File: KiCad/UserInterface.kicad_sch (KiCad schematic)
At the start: 0 parts

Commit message: Filled in schematic
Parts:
- added C13, C14, C15, C16, C17, C18, C19: C, symbol Device:C
- added D4, D5: LED, symbol Device:LED
- added J3: Btn_Menu_Conn, symbol Connector:Conn_01x06_Socket
- added J4: Btn_Matrix_Conn, symbol Connector:Conn_01x08_Socket
- added J5: Enc_Conn, Connector_PinHeader_2.54mm:PinHeader_1x03_P2.54mm_Vertical, symbol Connector:Conn_01x03_Socket
- added J6: Pwr_Conn, symbol Connector:Conn_01x02_Socket
- added J7: LCD_Conn, Connector_PinHeader_2.54mm:PinHeader_1x03_P2.54mm_Vertical, symbol Connector:Conn_01x03_Socket
- added R29, R30, R31, R32, R33, R34, R35: 10k, symbol Device:R
- added R36, R37: 1k, symbol Device:R
- added SW1, SW18, SW20, SW21: SW_Push, symbol Switch:SW_Push
- added SW10, SW11, SW12, SW13, SW14, SW15, SW16, SW17, SW2, SW3, SW4, SW5, SW6, SW7, SW8, SW9: SW_Push_45deg, symbol Switch:SW_Push_45deg
- added SW19: RotaryEncoder_Switch, symbol Device:RotaryEncoder_Switch
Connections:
- new net: SW13.1, SW17.1, SW5.1, SW9.1
- new net: SW14.2, SW15.2, SW16.2, SW17.2
- new net: SW11.1, SW15.1, SW3.1, SW7.1
- new net: SW10.2, SW11.2, SW12.2, SW13.2
- new net: SW12.1, SW16.1, SW4.1, SW8.1
- new net: SW2.2, SW3.2, SW4.2, SW5.2
- new net: D4.2 (A), R37.2
- new net: SW6.2, SW7.2, SW8.2, SW9.2
- new net: D5.2 (A), R36.2
- new net +3V3: J6.1 (Pin_1), R29.1, R30.1, R31.1, R32.1, R33.1, R34.1, R35.1
- new net ENC_CLK: C14.1, J5.1 (Pin_1), R30.2, SW19.A
- new net ENC_DT: C15.1, J5.2 (Pin_2), R31.2, SW19.B
- new net ENC_SW: C13.1, J5.3 (Pin_3), R29.2, SW19.S1
- new net GND: C13.2, C14.2, C15.2, C16.2, C17.2, C18.2, C19.2, D4.1 (K), D5.1 (K), J6.2 (Pin_2), SW1.1, SW18.1, SW19.C, SW19.S2, SW20.1, SW21.1
- new net LED1_IN: J3.5 (Pin_5), R37.1
- new net LED2_IN: J3.6 (Pin_6), R36.1
- new net SW1_OUT: C16.1, J3.1 (Pin_1), R32.2, SW1.2
- new net SW2_OUT: C17.1, J3.2 (Pin_2), R33.2, SW18.2
- new net SW3_OUT: C18.1, J3.3 (Pin_3), R34.2, SW20.2
- new net SW4_OUT: C19.1, J3.4 (Pin_4), R35.2, SW21.2
- new net X0: SW10.1, SW14.1, SW2.1, SW6.1
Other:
- note added: "Button Matrix"

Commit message: minor changes
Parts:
- C13, C14, C15, C16, C17, C18, C19, D4, D5, R29, R30, R31, R32, R33, R34, R35, R36, R37, SW1, SW10, SW11, SW12, SW13, SW14, SW15, SW16, SW17, SW18, SW19, SW2, SW20, SW21, SW3, SW4, SW5, SW6, SW7, SW8, SW9: now not fitted
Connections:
- net X0: now also J4.1 (Pin_1)
- net X3: now reaches SW13.1, SW17.1, SW5.1, SW9.1
- net X3: now also J4.4 (Pin_4)
- net Y3: now reaches SW14.2, SW15.2, SW16.2, SW17.2
- net Y3: now also J4.8 (Pin_8)
- net X1: now reaches J4.2 (Pin_2)
- net X1: now also SW11.1, SW15.1, SW3.1, SW7.1
- net X2: now reaches J4.3 (Pin_3)
- net X2: now also SW12.1, SW16.1, SW4.1, SW8.1
- net Y0: now reaches J4.5 (Pin_5)
- net Y0: now also SW2.2, SW3.2, SW4.2, SW5.2
- net Y1: now reaches J4.6 (Pin_6)
- net Y1: now also SW6.2, SW7.2, SW8.2, SW9.2
- net Y2: now reaches J4.7 (Pin_7)
- net Y2: now also SW10.2, SW11.2, SW12.2, SW13.2
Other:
- moved on the sheet: J3

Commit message: mux in ui
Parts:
- removed C18, C19: C, symbol Device:C
- removed D5: LED, symbol Device:LED
- removed R34, R35: 10k, symbol Device:R
- removed R36: 1k, symbol Device:R
- removed SW20, SW21: SW_Push, symbol Switch:SW_Push
- added U8: CD4051B, symbol Analog_Switch:CD4051B
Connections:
- net +3V3: now also U8.16 (VDD)
- net GND: now also U8.6 (INH), U8.7 (VEE), U8.8 (VSS)
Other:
- moved on the sheet: J4, SW10, SW11, SW12, SW13, SW14, SW15, SW16, SW17, SW2, SW3, SW4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

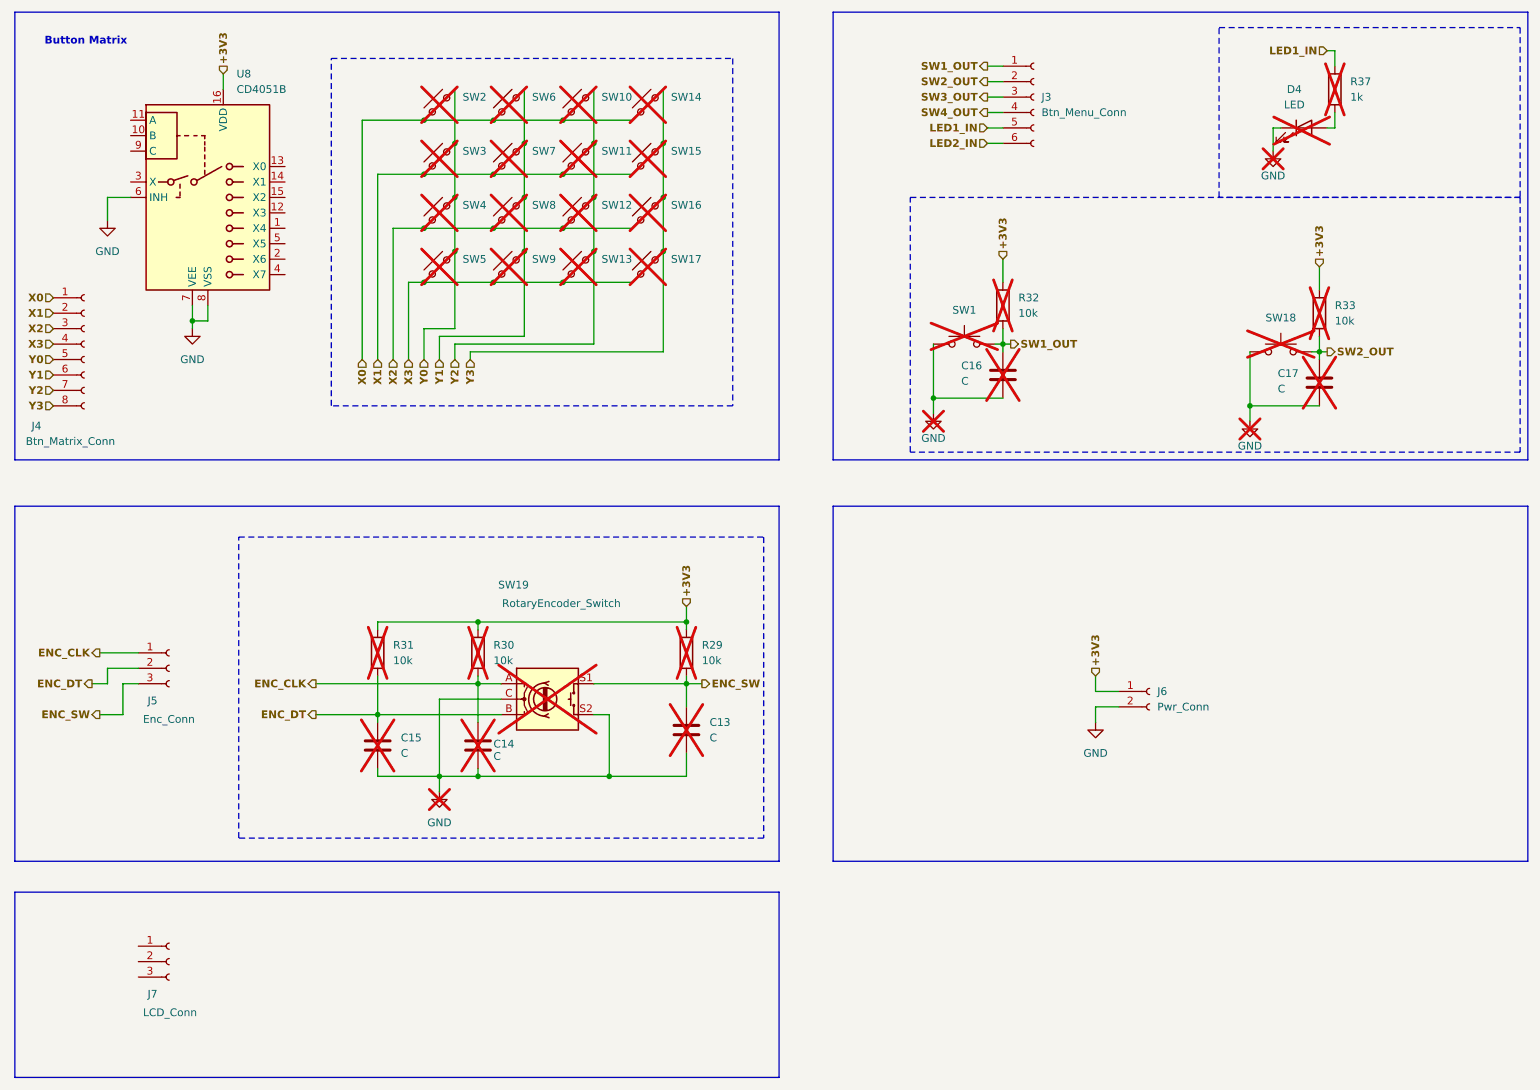
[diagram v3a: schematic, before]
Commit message: UI connections to uC
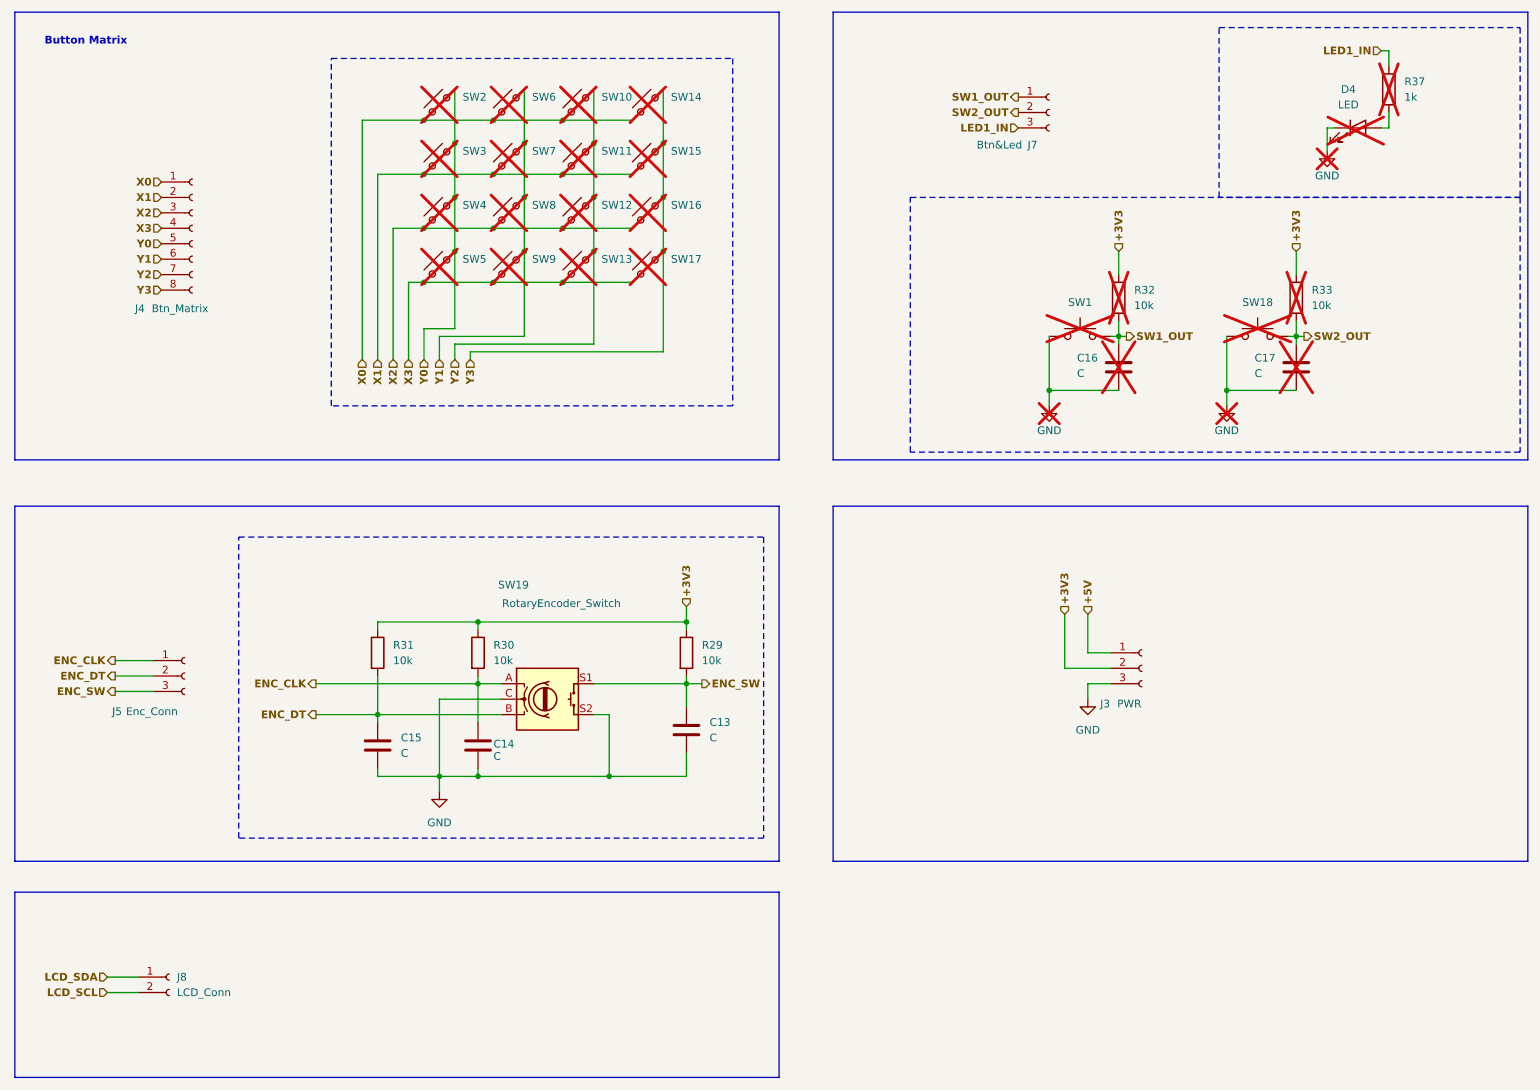
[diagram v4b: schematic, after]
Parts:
- removed J3: Btn_Menu_Conn, symbol Connector:Conn_01x06_Socket
- removed J6: Pwr_Conn, symbol Connector:Conn_01x02_Socket
- removed U8: CD4051B, symbol Analog_Switch:CD4051B
- added J3: PWR, Connector_PinHeader_2.54mm:PinHeader_1x03_P2.54mm_Vertical, symbol Connector:Conn_01x03_Socket
- added J8: LCD_Conn, Connector_PinHeader_2.54mm:PinHeader_1x02_P2.54mm_Vertical, symbol Connector:Conn_01x02_Socket
- C13, C14, C15, R29, R30, R31, SW19: now fitted
- D4, SW1, SW18: now left out of the parts list
- J4: value Btn_Matrix_Conn -> Btn_Matrix; footprint (none) -> Connector_PinSocket_2.54mm:PinSocket_1x08_P2.54mm_Vertical
- J7: value LCD_Conn -> Btn&Led
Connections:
- net +3V3: now also J3.2 (Pin_2)
- net GND: now also J3.3 (Pin_3)
- net LED1_IN: now also J7.3 (Pin_3)
- net SW1_OUT: now also J7.1 (Pin_1)
- net SW2_OUT: now also J7.2 (Pin_2)
- new net +5V: J3.1 (Pin_1)
- new net LCD_SCL: J8.2 (Pin_2)
- new net LCD_SDA: J8.1 (Pin_1)
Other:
- moved on the sheet: C16, C17, D4, J4, J5, R32, R33, R37, SW1, SW18

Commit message: First DAC layout, rough board layout
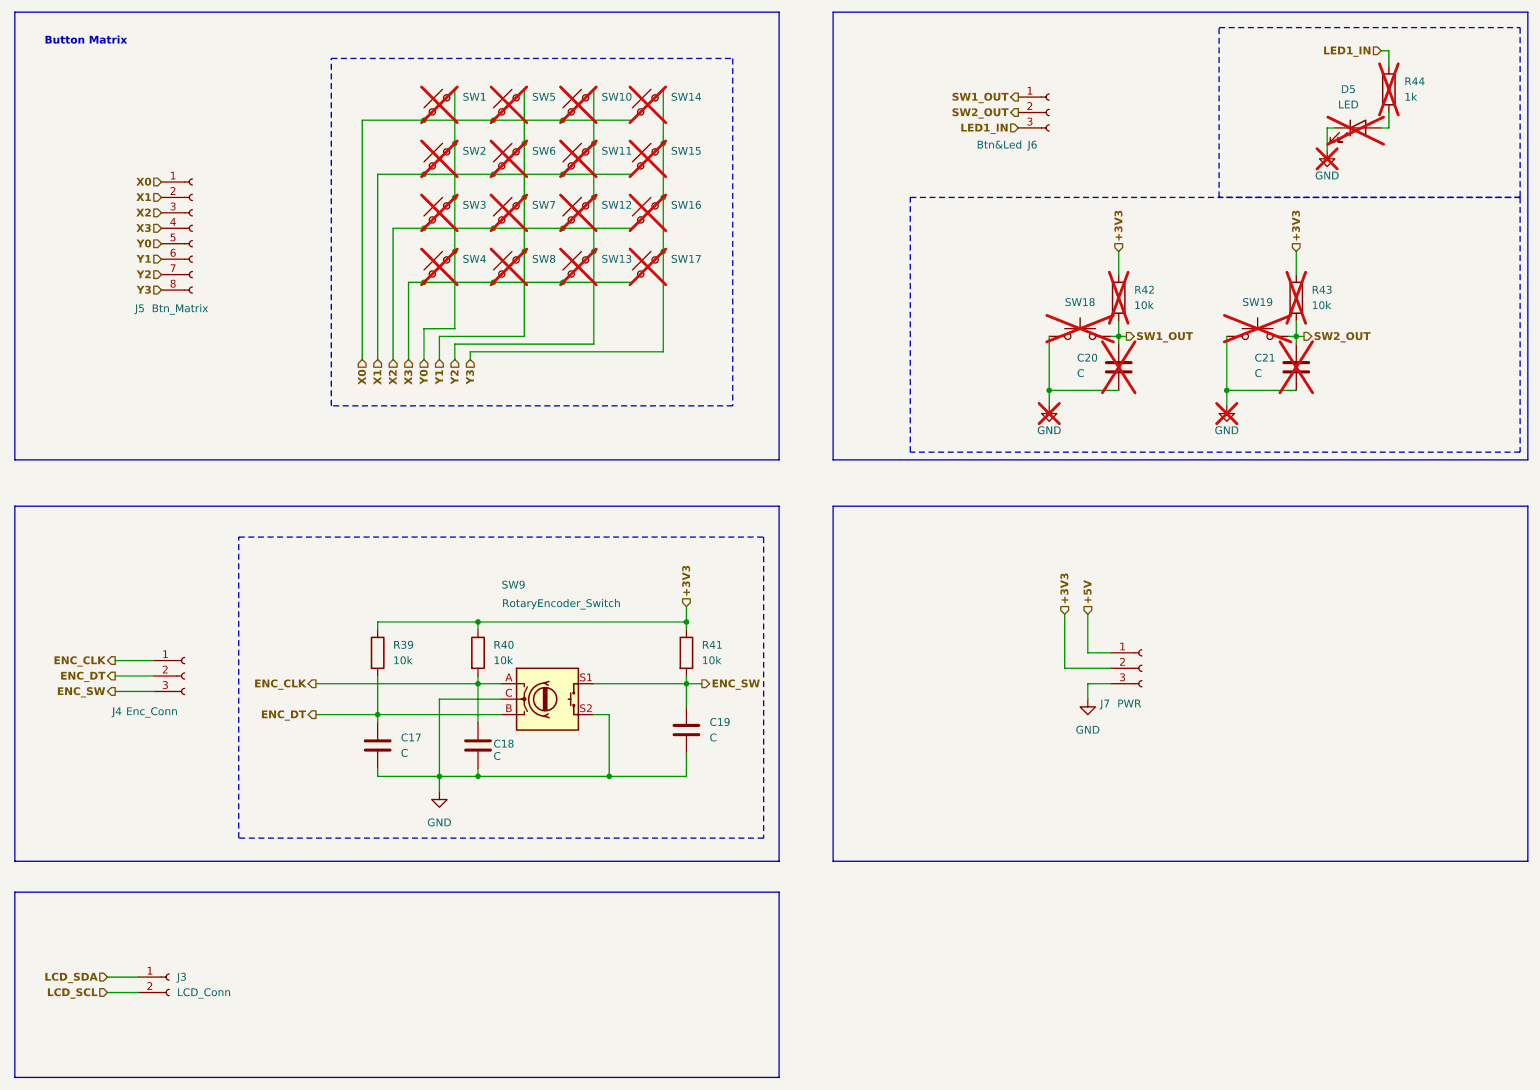
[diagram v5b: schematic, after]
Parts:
- renumbered C15 to C17, C14 to C18, C13 to C19, C16 to C20, C17 to C21, D4 to D5, J8 to J3, J5 to J4, J4 to J5, J7 to J6, J3 to J7, R31 to R39, R30 to R40, R29 to R41, R32 to R42, R33 to R43, R37 to R44, SW2 to SW1, SW1 to SW18, SW18 to SW19, SW3 to SW2, SW4 to SW3, SW5 to SW4, SW6 to SW5, SW7 to SW6, SW8 to SW7, SW9 to SW8, SW19 to SW9

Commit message: minor changes, testing
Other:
- moved on the sheet: J5
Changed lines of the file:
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@@
 	(hierarchical_label "Y0"
 		(shape input)
-		(at 44.45 55.88 180)
+		(at 39.37 38.1 180)
 		(fields_autoplaced yes)
 		(effects
@@
 	(hierarchical_label "Y1"
 		(shape input)
-		(at 44.45 58.42 180)
+		(at 39.37 40.64 180)
 		(fields_autoplaced yes)
 		(effects
@@
 	(hierarchical_label "X3"
 		(shape input)
-		(at 44.45 53.34 180)
+		(at 39.37 35.56 180)
 		(fields_autoplaced yes)
 		(effects
@@
 	(hierarchical_label "Y3"
 		(shape input)
-		(at 44.45 63.5 180)
+		(at 39.37 45.72 180)
 		(fields_autoplaced yes)
 		(effects
@@
 	(hierarchical_label "Y2"
 		(shape input)
-		(at 44.45 60.96 180)
+		(at 39.37 43.18 180)
 		(fields_autoplaced yes)
 		(effects
@@
 	(hierarchical_label "X0"
 		(shape input)
-		(at 44.45 45.72 180)
+		(at 39.37 27.94 180)
 		(fields_autoplaced yes)
 		(effects
@@
 	(hierarchical_label "X1"
 		(shape input)
-		(at 44.45 48.26 180)
+		(at 39.37 30.48 180)
 		(fields_autoplaced yes)
 		(effects
@@
 	(hierarchical_label "X2"
 		(shape input)
-		(at 44.45 50.8 180)
+		(at 39.37 33.02 180)
 		(fields_autoplaced yes)
 		(effects
@@
 	(symbol
 		(lib_id "Connector:Conn_01x08_Socket")
-		(at 49.53 53.34 0)
+		(at 44.45 35.56 0)
 		(unit 1)
 		(exclude_from_sim no)
@@
 		(dnp no)
 		(property "Reference" "J5"
-			(at 40.894 66.548 0)
+			(at 35.814 48.768 0)
 			(effects
 				(font
@@
 		)
 		(property "Value" "Btn_Matrix"
-			(at 47.498 66.548 0)
+			(at 42.418 48.768 0)
 			(effects
 				(font
@@
 		)
 		(property "Footprint" "Connector_PinSocket_2.54mm:PinSocket_1x08_P2.54mm_Vertical"
-			(at 49.53 53.34 0)
+			(at 44.45 35.56 0)
 			(effects
 				(font
@@
 		)
 		(property "Datasheet" "~"
-			(at 49.53 53.34 0)
+			(at 44.45 35.56 0)
 			(effects
 				(font
@@
 		)
 		(property "Description" "Generic connector, single row, 01x08, script generated"
-			(at 49.53 53.34 0)
-			(effects
-				(font
+			(at 44.45 35.56 0)
+			(effects
+				(font
